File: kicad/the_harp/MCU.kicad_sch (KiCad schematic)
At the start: 23 parts, among them U201 STM32H750VBT6, U202 W25Q128JVSIQ, Y201 25MHz 9pF

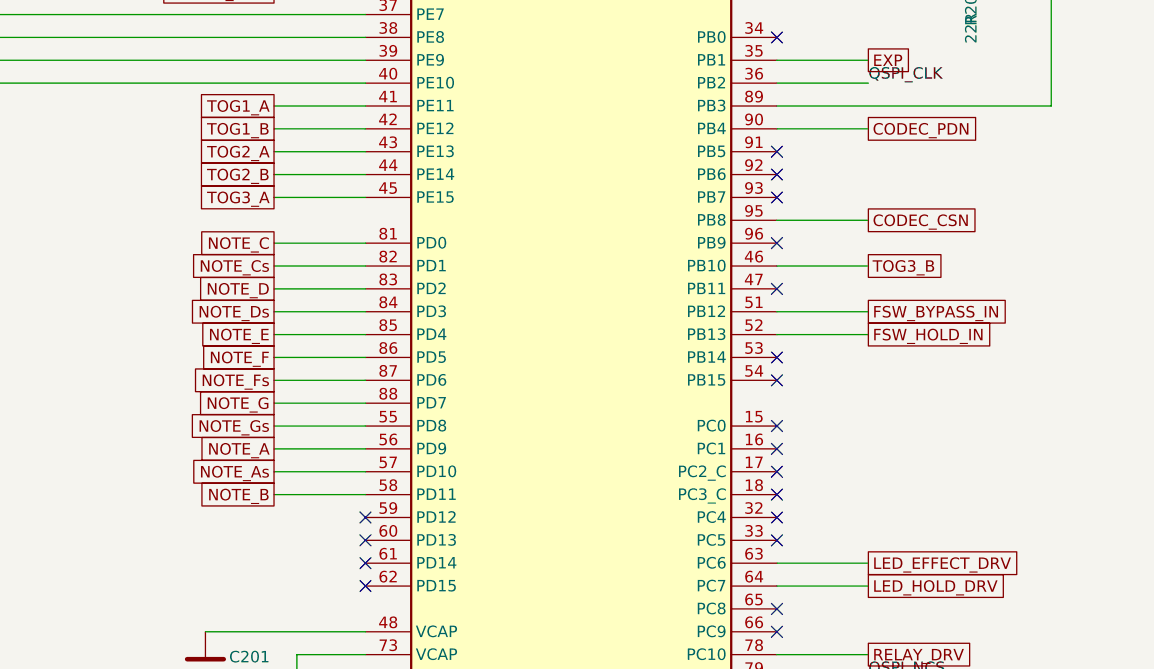
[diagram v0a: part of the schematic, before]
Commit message: Stereo single-ended input and an OLED display
IN becomes a TRS jack (tip left, ring right) with a second OPA2365 buffer and
THS4522 channel B into the AK4621EF's AINR; the codec inputs are no longer
parked. A mono plug is detected by the right channel reading silence. The
twelve note LEDs and R107-R118 give way to a 0.91 in I2C OLED connector (J408,
PB6/PB7) with 4.7k pull-ups. Schematic regenerated (190 parts, netlist OK on
all sheets); design brief, PCB plan, firmware requirements and the design
report updated. The PCB still carries the old LED footprints until Update PCB
from Schematic is run in KiCad.

Co-Authored-By: Claude Sonnet 5.5 <noreply@anthropic.com>
Claude-Session: https://claude.ai/code/session_016hDejPHPgG8auBLMyByYZK
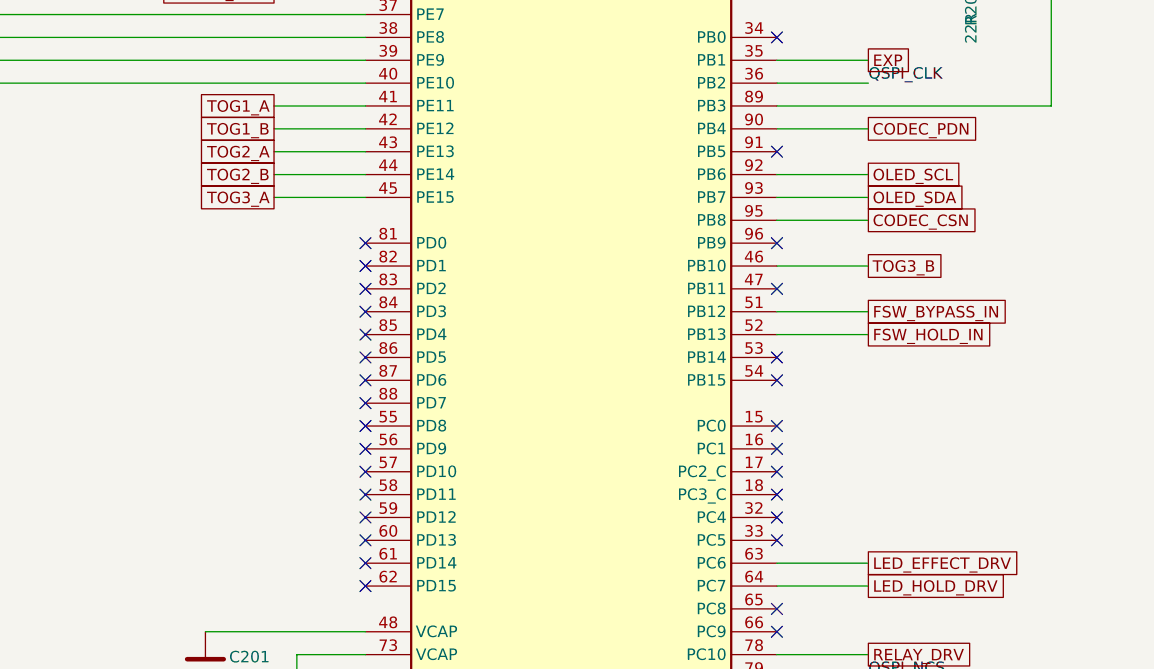
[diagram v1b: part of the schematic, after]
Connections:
- net OLED_SCL: now reaches U201.92 (PB6)
- net OLED_SDA: now reaches U201.93 (PB7)
- net NOTE_A: no longer names the net of U201.56 (PD9)
- net NOTE_As: no longer names the net of U201.57 (PD10)
- net NOTE_B: no longer names the net of U201.58 (PD11)
- net NOTE_C: no longer names the net of U201.81 (PD0)
- net NOTE_Cs: no longer names the net of U201.82 (PD1)
- net NOTE_D: no longer names the net of U201.83 (PD2)
- net NOTE_Ds: no longer names the net of U201.84 (PD3)
- net NOTE_E: no longer names the net of U201.85 (PD4)
- net NOTE_F: no longer names the net of U201.86 (PD5)
- net NOTE_Fs: no longer names the net of U201.87 (PD6)
- net NOTE_G: no longer names the net of U201.88 (PD7)
- net NOTE_Gs: no longer names the net of U201.55 (PD8)
- no-connect marks 34 -> 44
